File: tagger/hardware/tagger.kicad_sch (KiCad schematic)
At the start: 35 parts, among them J4 SWD, J7 TETHER_DATA, J8 DISPLAY, J9 IO_CONN, Q1 Q_NMOS_GSD, SW24 BOOT0, SW26 NRST, U2 STM32F103RGTx, U4 ST3485EB, Y3 CG04874-8M

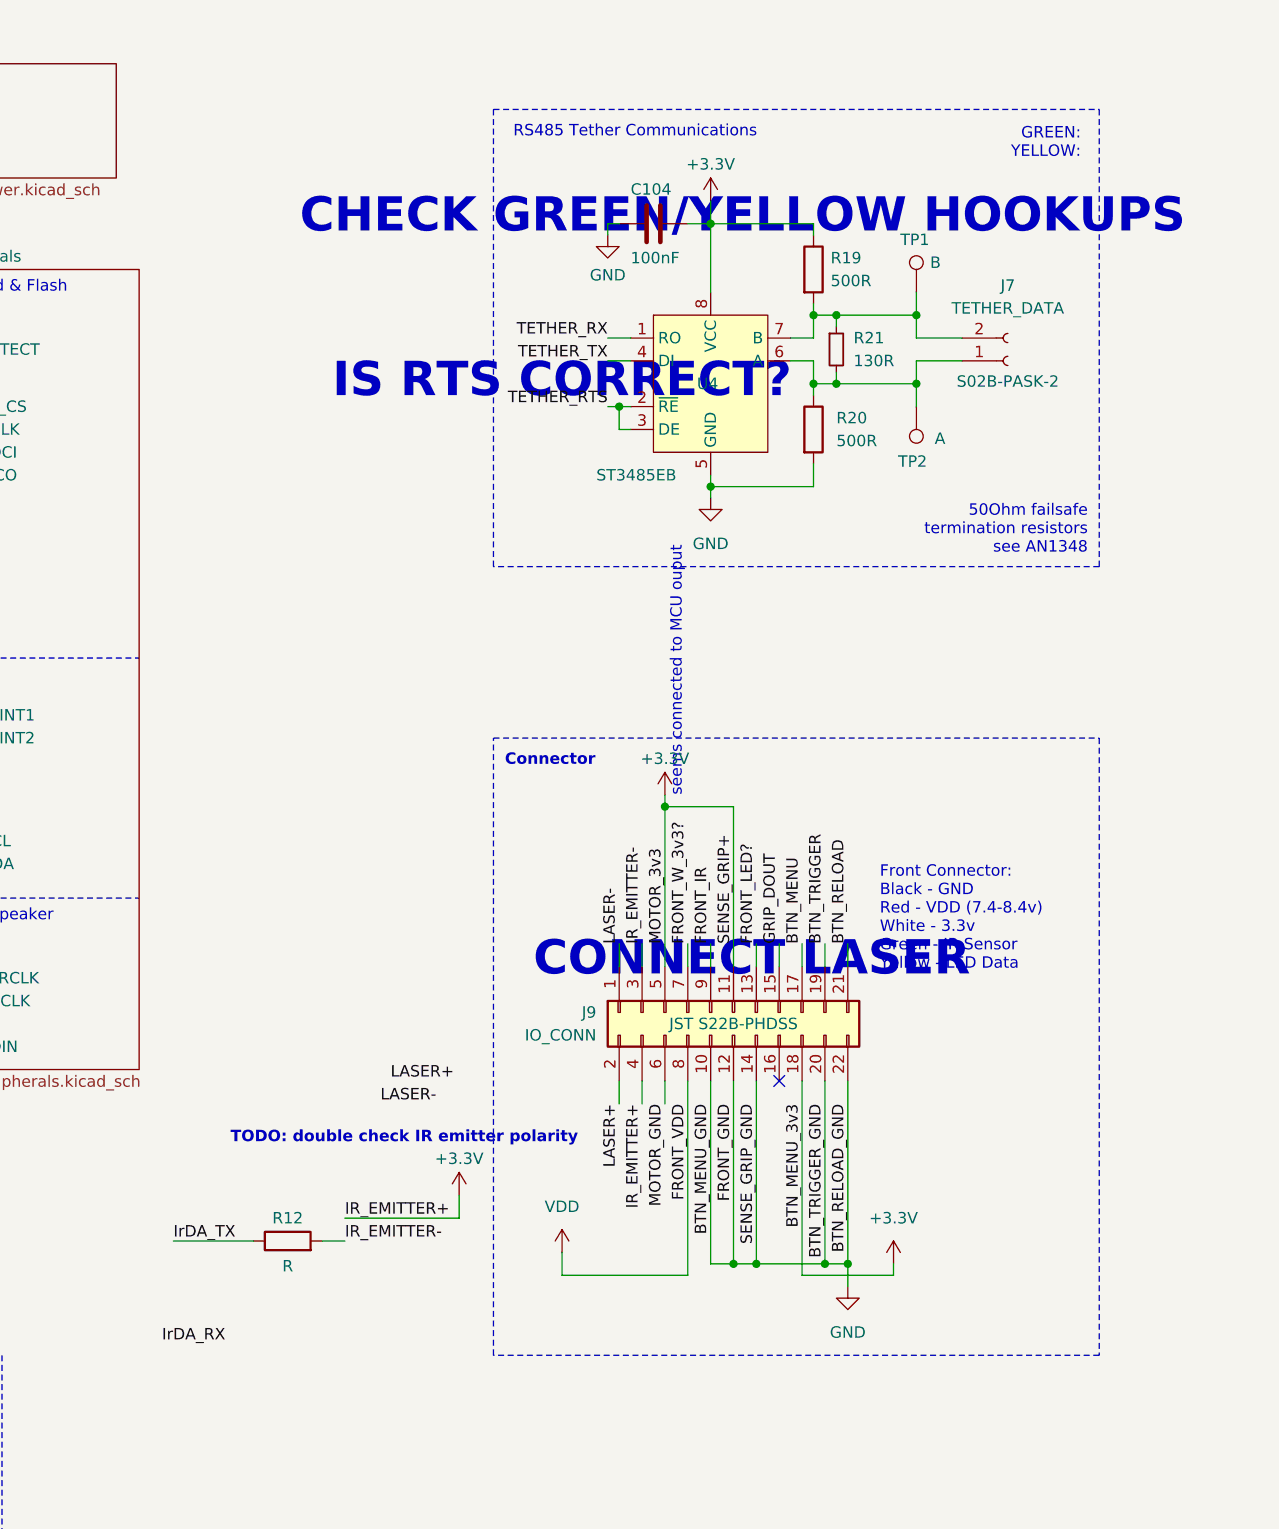
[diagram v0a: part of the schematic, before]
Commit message: feat: audio routing and test points
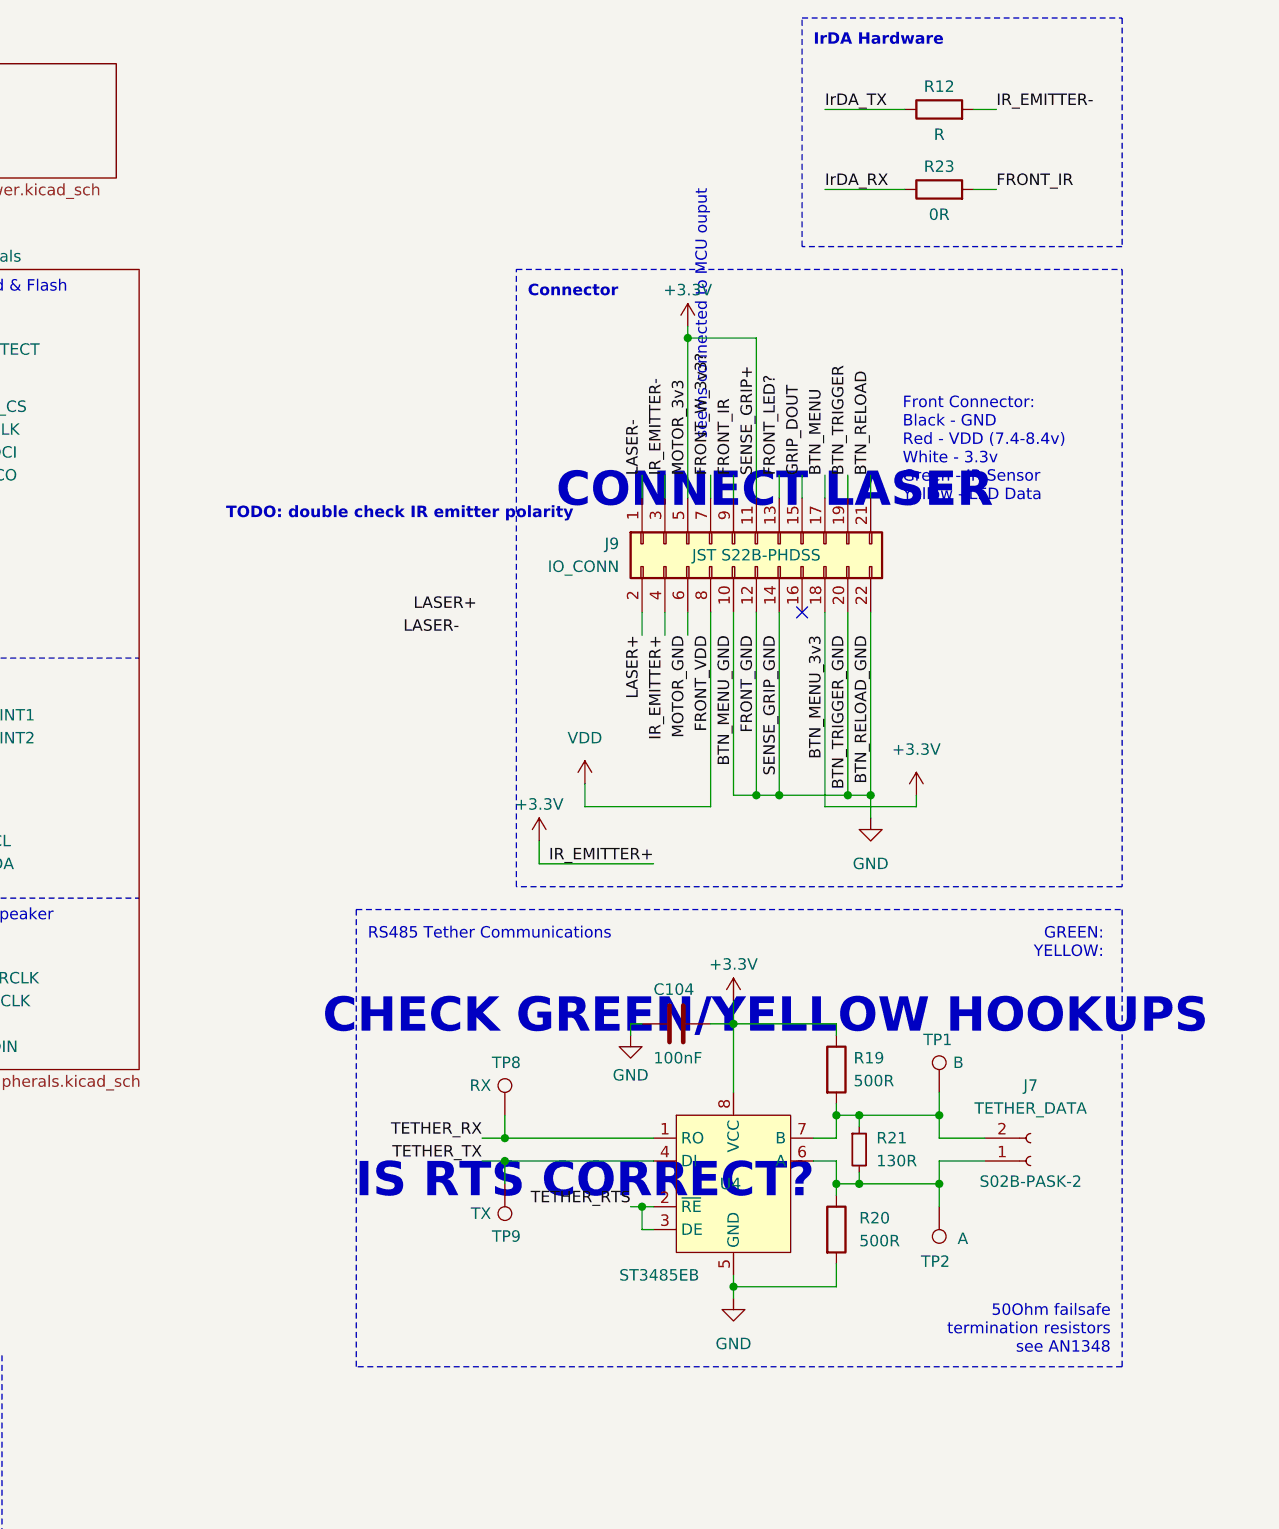
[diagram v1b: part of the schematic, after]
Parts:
- added R23: 0R, Resistor_SMD:R_0402_1005Metric, symbol Device:R
- added TP8: RX, TestPoint:TestPoint_Bridge_Pitch2.54mm_Drill1.0mm, symbol Connector:TestPoint
- added TP9: TX, TestPoint:TestPoint_Bridge_Pitch2.54mm_Drill1.0mm, symbol Connector:TestPoint
- R12: footprint (none) -> Resistor_SMD:R_0402_1005Metric
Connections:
- net FRONT_IR: now also R23.2
- net IrDA_RX: now also R23.1
- net TETHER_RX: now also TP8.1
- net TETHER_TX: now also TP9.1
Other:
- note added: "IrDA Hardware"
- moved on the sheet: C104, J7, J9, R12, R19, R20, R21, TP1, TP2, U4

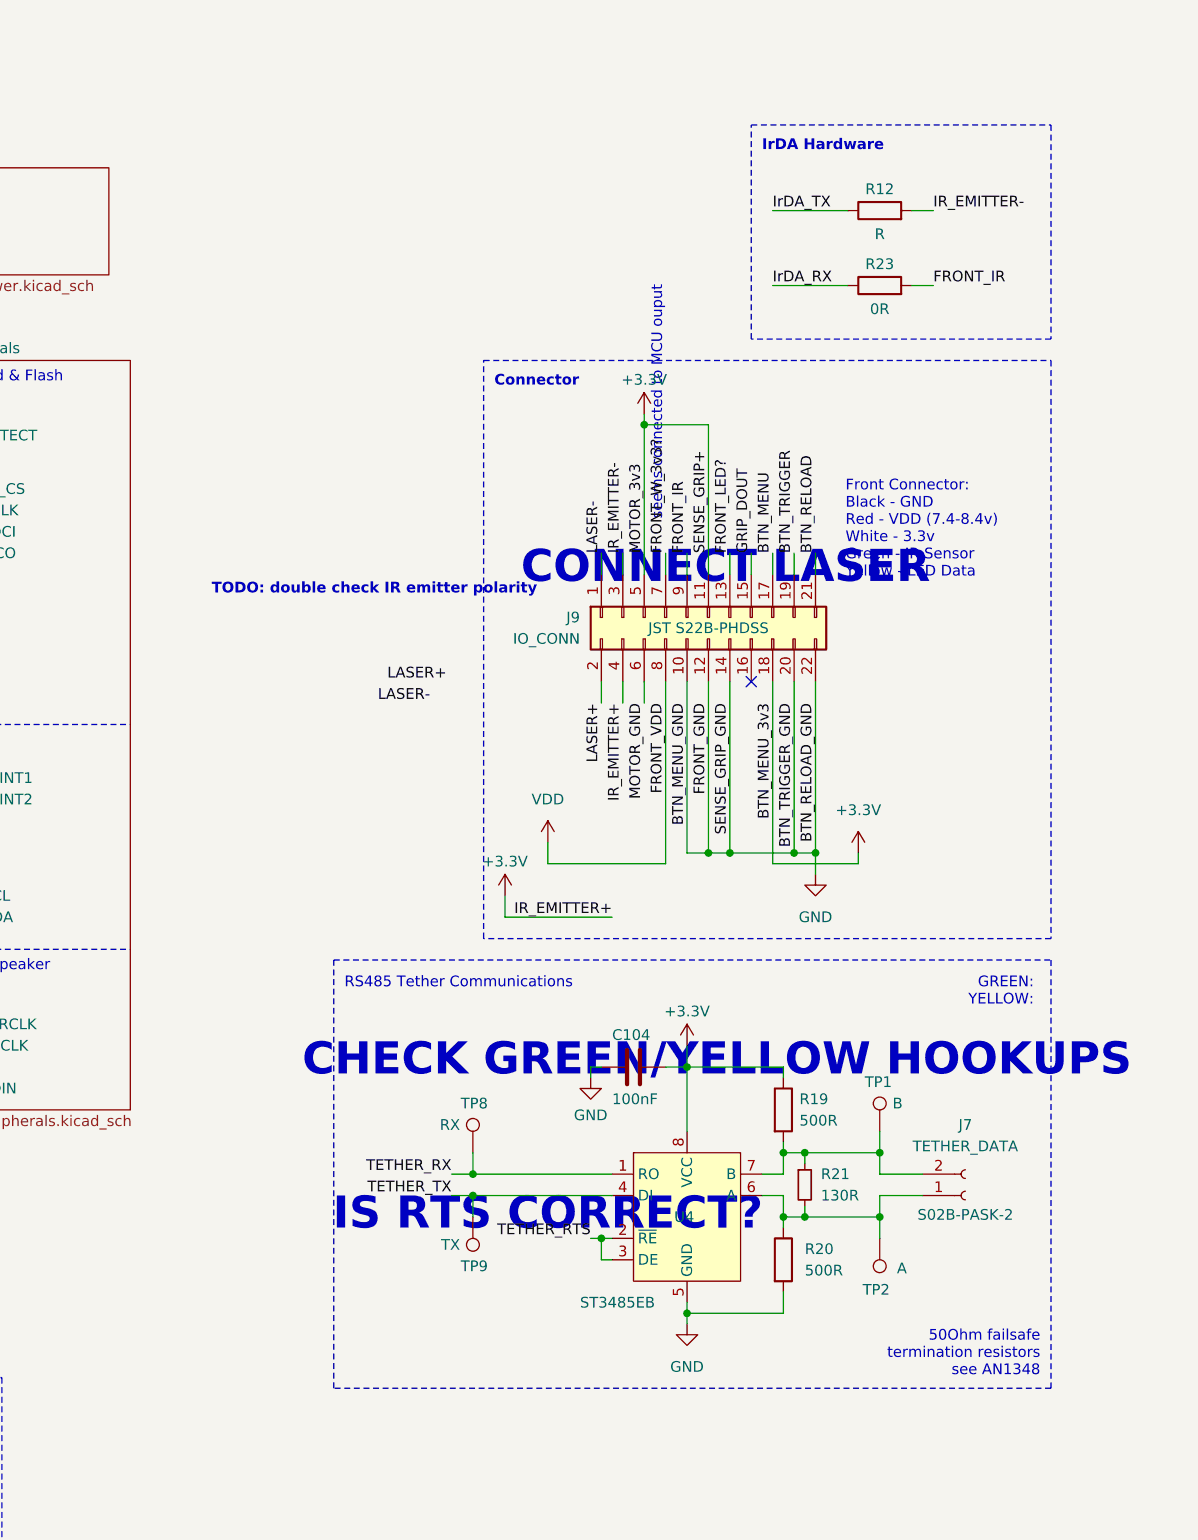
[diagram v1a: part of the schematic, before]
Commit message: feat: replace tether comms with full-duplex
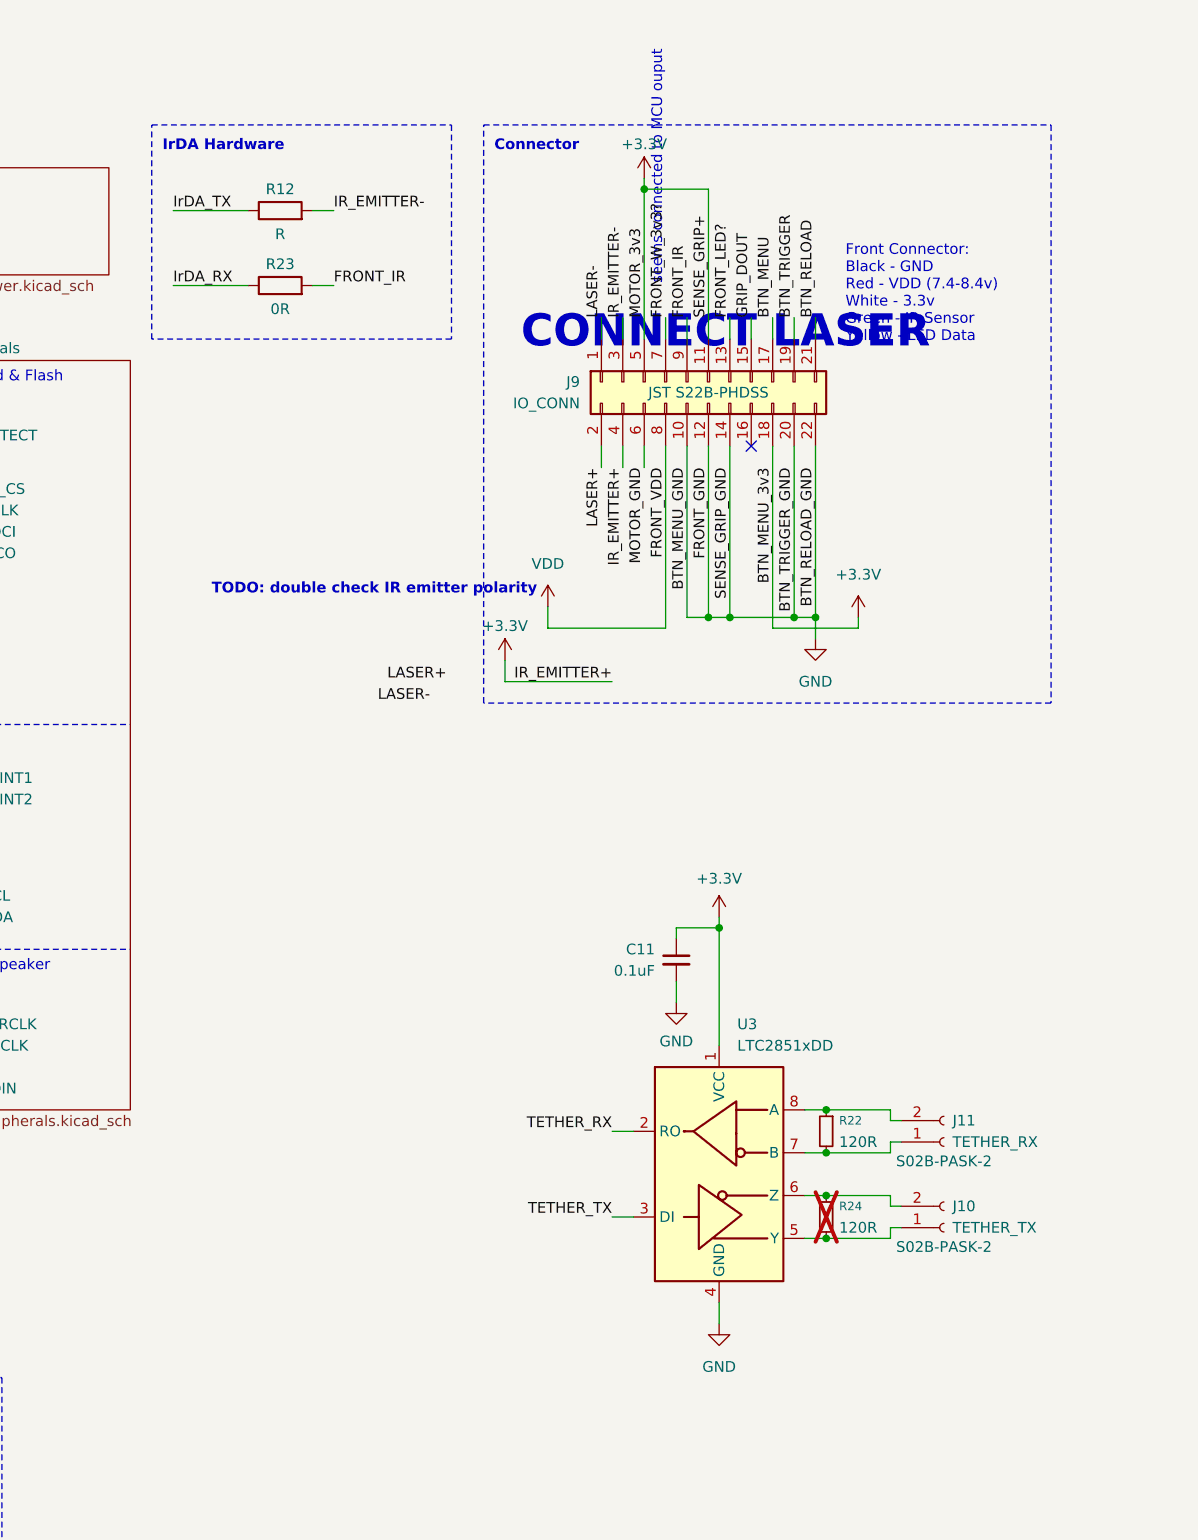
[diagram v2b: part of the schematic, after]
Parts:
- removed C104: 100nF, Capacitor_SMD:C_0402_1005Metric, symbol Device:C
- removed J7: TETHER_DATA, tagger:S02B-PASK-2, symbol Connector:Conn_01x02_Socket
- removed R19, R20: 500R, Resistor_SMD:R_0402_1005Metric, symbol Device:R
- removed R21: 130R, Resistor_SMD:R_0402_1005Metric, symbol Device:R_Small
- removed TP1: B, TestPoint:TestPoint_Bridge_Pitch2.54mm_Drill1.0mm, symbol Connector:TestPoint
- removed TP2: A, TestPoint:TestPoint_Bridge_Pitch2.54mm_Drill1.0mm, symbol Connector:TestPoint
- removed TP8: RX, TestPoint:TestPoint_Bridge_Pitch2.54mm_Drill1.0mm, symbol Connector:TestPoint
- removed TP9: TX, TestPoint:TestPoint_Bridge_Pitch2.54mm_Drill1.0mm, symbol Connector:TestPoint
- removed U4: ST3485EB, Package_SO:SOIC-8_3.9x4.9mm_P1.27mm, symbol ST3485EBDR:ST3485EBDR
- added C11: 0.1uF, symbol Device:C_Small
- added J10: TETHER_TX, tagger:S02B-PASK-2, symbol Connector:Conn_01x02_Socket
- added J11: TETHER_RX, tagger:S02B-PASK-2, symbol Connector:Conn_01x02_Socket
- added R22, R24: 120R, symbol Device:R_Small
- added U3: LTC2851xDD, Package_DFN_QFN:DFN-8-1EP_3x3mm_P0.5mm_EP1.66x2.38mm, symbol Interface_UART:LTC2851xDD
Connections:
- net +3.3V: now also C11.1, U3.1 (VCC)
- net GND: now also C11.2, U3.4 (GND), U3.9 (GND)
- net TETHER_RX: now also U3.2 (RO)
- net TETHER_TX: now also U3.3 (DI)
- new net: J10.1 (Pin_1), R24.2, U3.5 (Y)
- new net: J10.2 (Pin_2), R24.1, U3.6 (Z)
- new net: J11.1 (Pin_1), R22.2, U3.7 (B)
- new net: J11.2 (Pin_2), R22.1, U3.8 (A)
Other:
- note removed: "50Ohm failsafe termination resistors see AN1348"
- note removed: "CHECK GREEN/YELLOW HOOKUPS"
- note removed: "GREEN: YELLOW:"
- note removed: "IS RTS CORRECT?"
- note removed: "RS485 Tether Communications"
- moved on the sheet: J9, R12, R23
